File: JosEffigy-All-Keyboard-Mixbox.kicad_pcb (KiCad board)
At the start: 2 copper layers, 186.7 x 123.2 mm, 55 parts, among them U1 Pico, U2 SN74LV1T34DBV

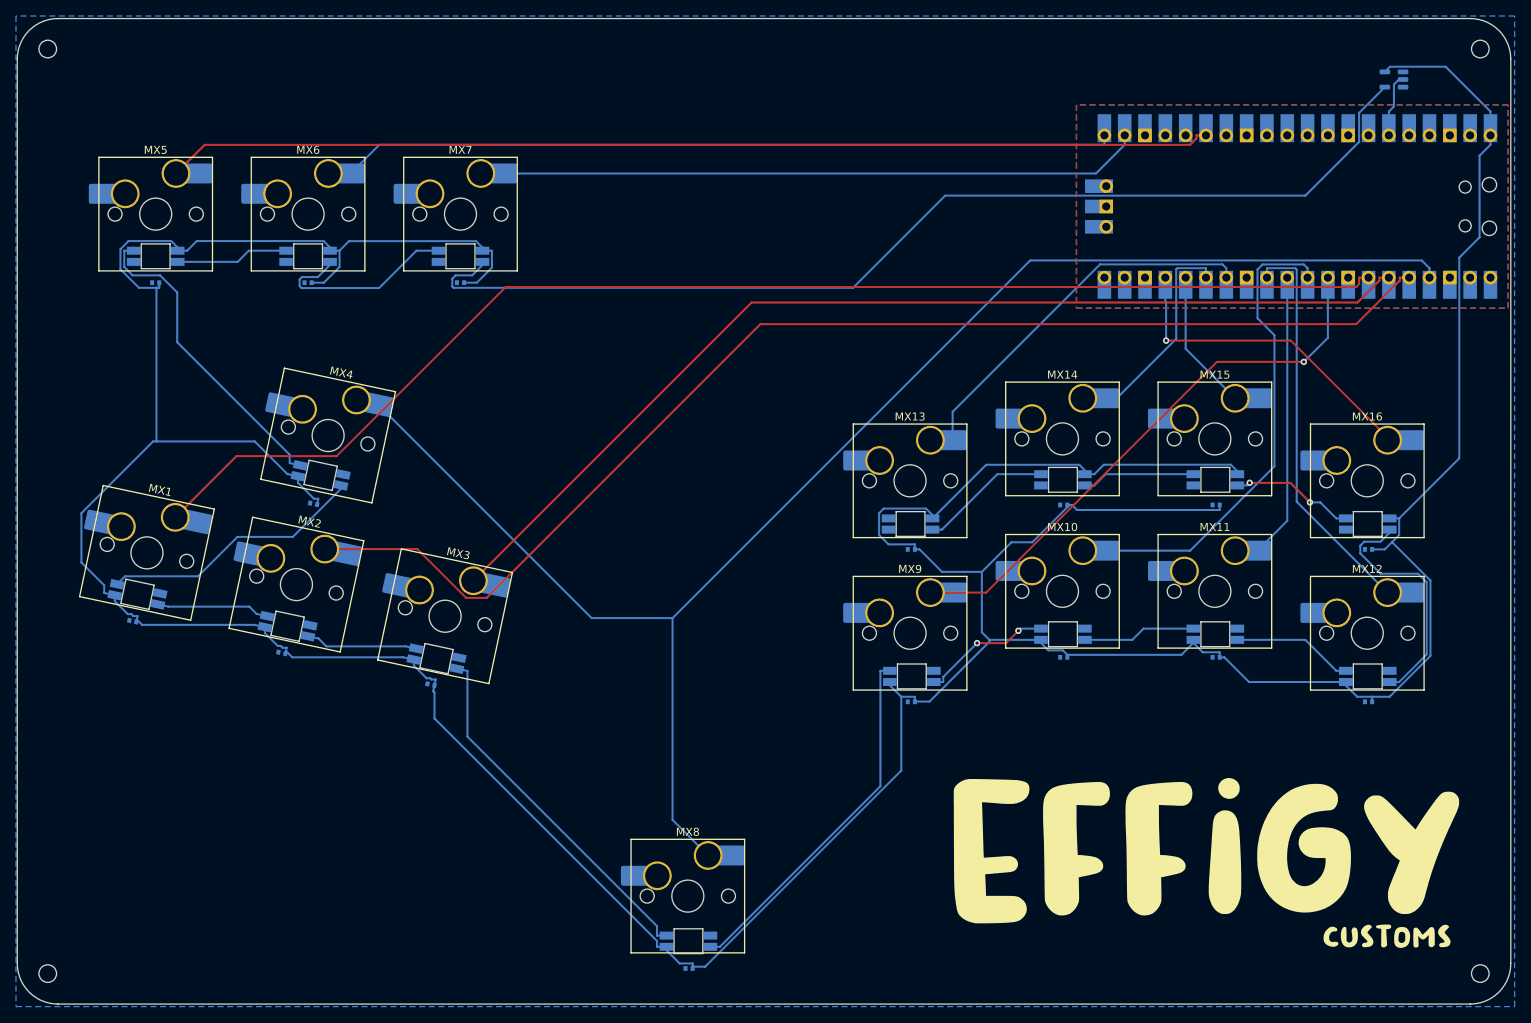
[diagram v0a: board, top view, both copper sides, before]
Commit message: Redid all routing manually
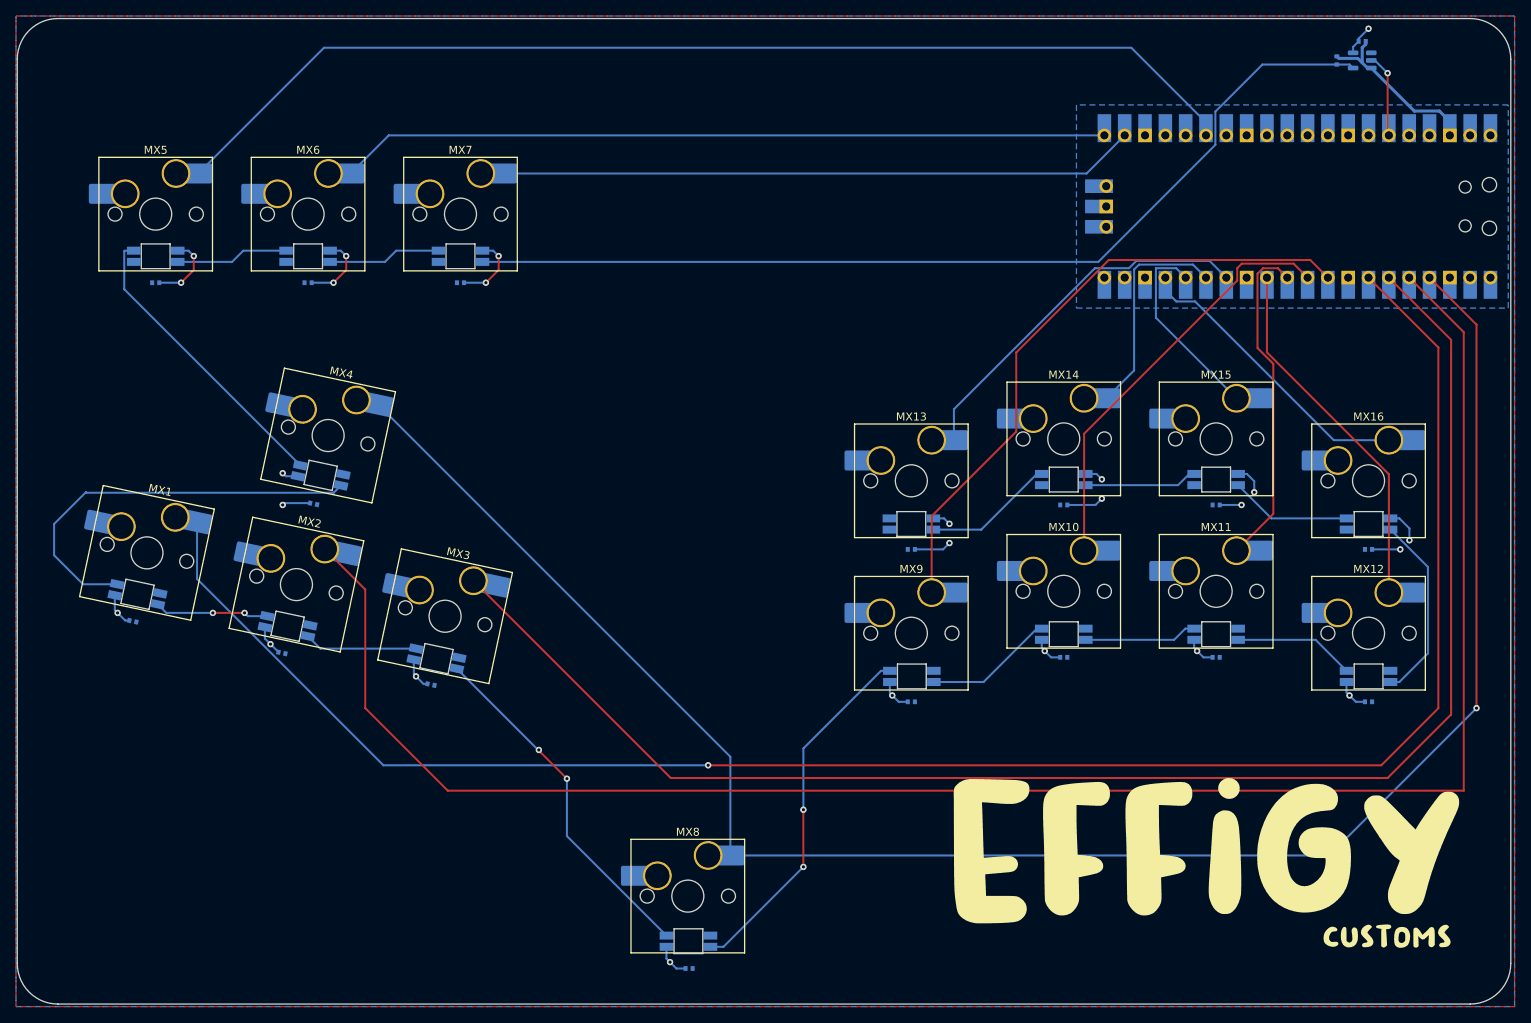
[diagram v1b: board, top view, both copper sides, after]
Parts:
- removed H1, H2, H3, H4: MountingHole_2.2mm_M2, MountingHole:MountingHole_2.2mm_M2
- added C17: 100nf, CAPC1005X55N:CAPC1005X55N, B.Cu at (215.1, 39.7)
- added R1: R, Resistor_SMD:R_0402_1005Metric, B.Cu at (211.9, 42.1)
- moved U2 4.63 mm to (215.1, 42.1)
- moved MX10 0.16 mm to (177.8, 108.4)
- moved MX12 0.16 mm to (215.9, 113.7)
- moved MX13 0.16 mm to (158.8, 94.6)
- moved MX14 0.16 mm to (177.8, 89.4)
- moved MX16 0.16 mm to (215.9, 94.6)
- moved MX9 0.16 mm to (158.8, 113.7)
- moved MX11 0.16 mm to (196.8, 108.4)
- moved MX15 0.16 mm to (196.8, 89.4)
- moved D14 0.11 mm to (177.8, 94.5)
- moved D15 0.11 mm to (196.8, 94.5)
- moved D12 0.10 mm to (215.9, 119.1)
- moved D13 0.10 mm to (158.8, 100.0)
- moved D16 0.10 mm to (215.9, 100.0)
- moved D10 0.10 mm to (177.8, 113.8)
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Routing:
- net VCC: track 572.2 -> 96.9 mm, vias 0 -> 25
- net DOWN: track 157.8 -> 230.5 mm
- net LEFT: track 165.0 -> 232.3 mm, vias 0 -> 1
- net RIGHT: track 133.3 -> 193.5 mm
- net UP: track 199.8 -> 231.7 mm, vias 0 -> 1
- net GND: track 0.00 -> 22.1 mm
- net Net-(D1-DIN): track 33.3 -> 51.2 mm
- net Net-(D7-DIN): track 135.0 -> 121.7 mm
- net Net-(D6-DIN): track 25.2 -> 14.1 mm
- net 2K: track 61.7 -> 53.0 mm
- net 4K: track 52.8 -> 45.7 mm
- net Net-(D12-DOUT): track 30.6 -> 23.6 mm
- net 1K: track 73.2 -> 79.1 mm, vias 1 -> 0
- net HOME: track 133.7 -> 138.0 mm
- net 3P: track 20.4 -> 24.6 mm
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- added copper zone on F.Cu, net VCC
- removed copper zone on F.Cu, net GND
